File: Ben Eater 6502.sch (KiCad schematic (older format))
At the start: 13 parts, among them J1 PS/2 Keyboard, SW1 Reset, SW2 NMI, U1 W65C02SxP, U2 4011, U3 28C256, U4 AS6C62256A, U5 W65C22SxP

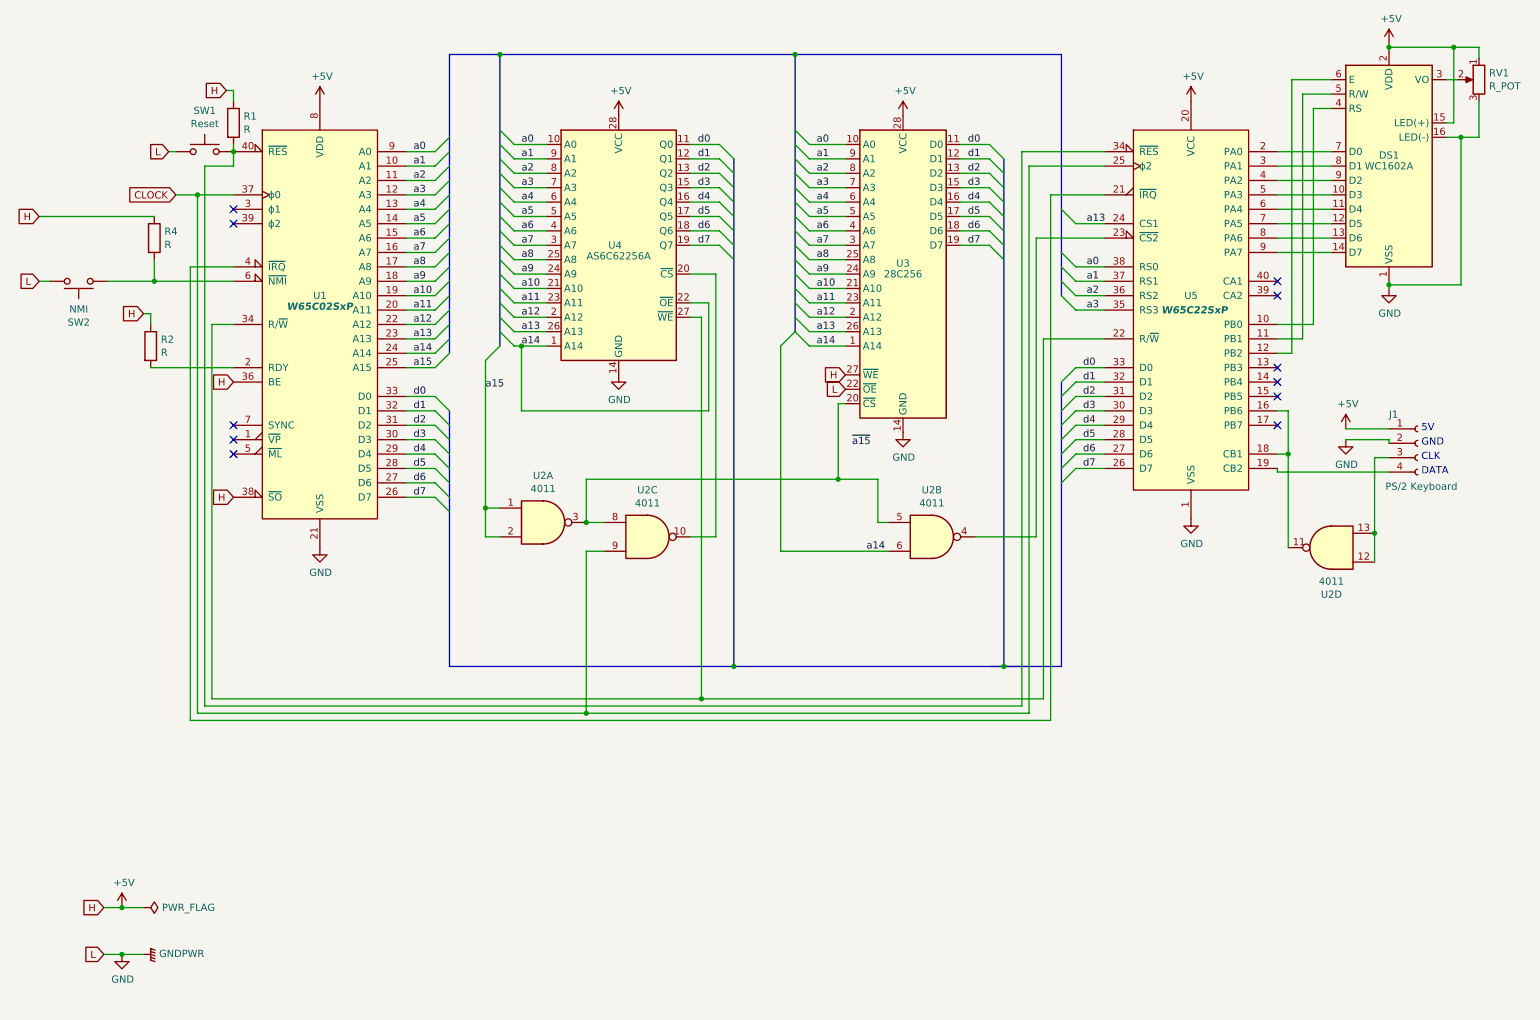
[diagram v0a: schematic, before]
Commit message: Add 74HC74 flip-flop to PS/2 keyboard data
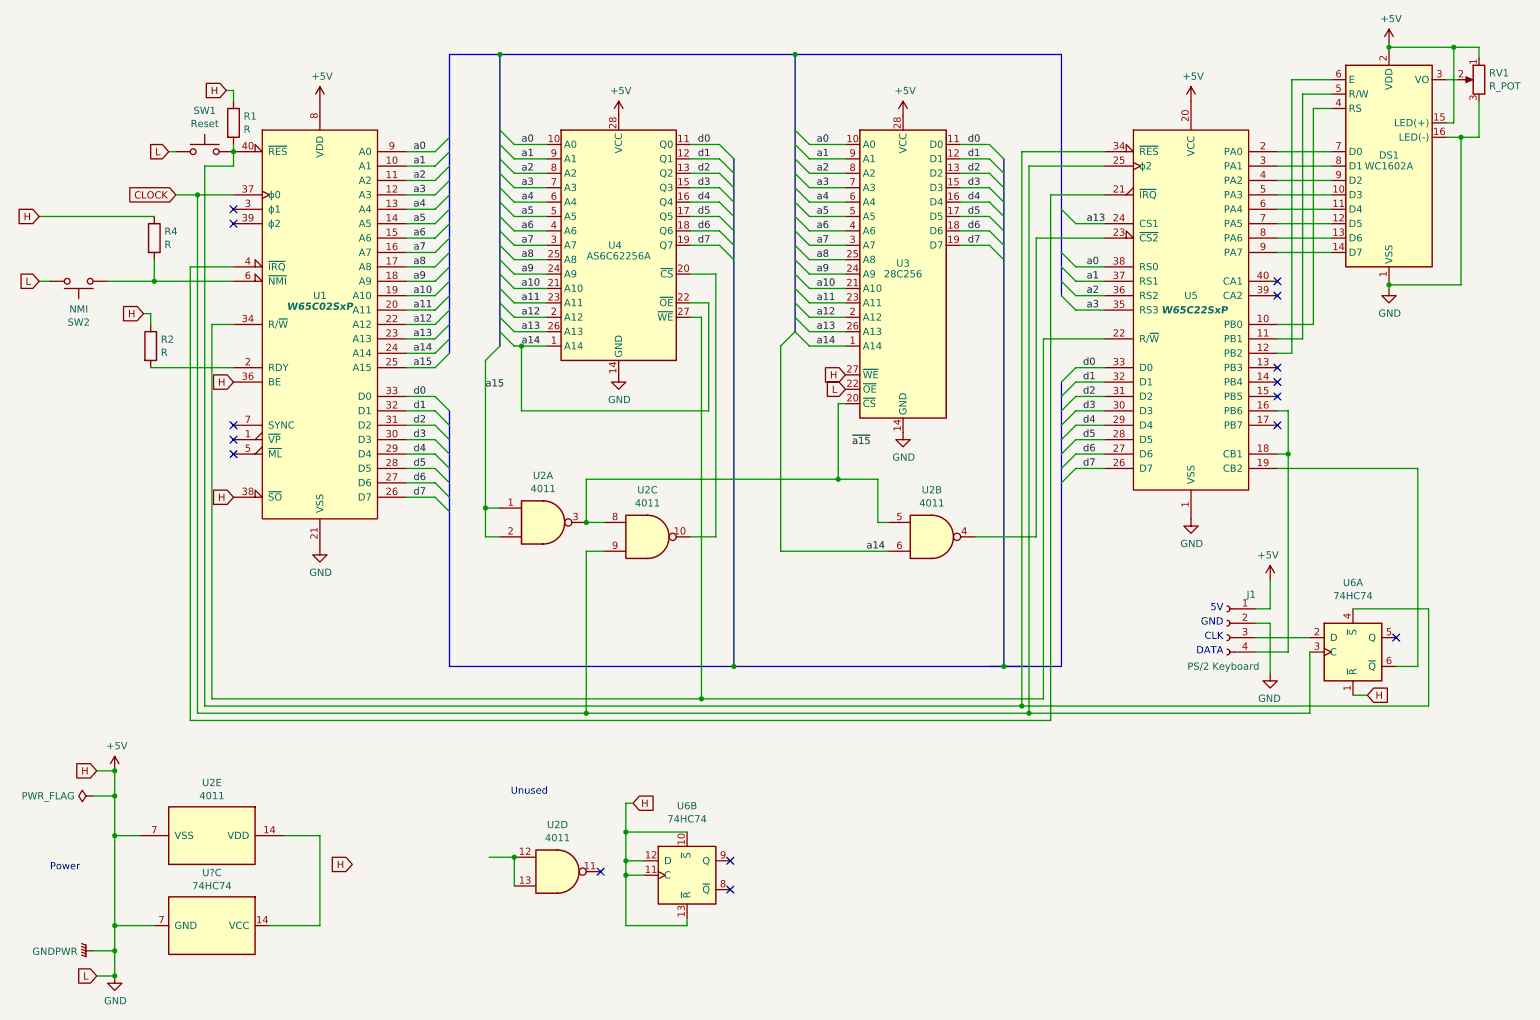
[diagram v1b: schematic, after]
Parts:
- added unit 5 of U2
- added U6, U?: 74HC74, symbol 74xx:74HC74
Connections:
- net GND is gone; now on net +5V: DS1.1 (VSS), DS1.16 (LED(-)), J1.2 (Pin_2), RV1.3, SW1.1, SW2.2, U1.21 (VSS), U3.14 (GND), U3.22 (~OE), U4.14 (GND), U5.1 (VSS)
- net +5V: now also U2.7 (VSS), U6.1 (~R), U6.10 (~S), U6.11 (C), U6.12 (D), U6.13 (~R), U?.7 (GND)
- net CLOCK: now also U6.3 (C)
- net at R1.2, SW1.2, U1.40 (~RES)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: now also U6.4 (~S)
- net at U5.16 (PB6), U5.18 (CB1): now also J1.4 (Pin_4); no longer U2.11
- net at U5.19 (CB2): now also U6.6 (~Q); no longer J1.4 (Pin_4)
- net at U2.12, U2.13: no longer J1.3 (Pin_3)
- new net: J1.3 (Pin_3), U6.2 (D)
- new net: U2.14 (VDD), U?.14 (VCC)
- no-connect marks 11 -> 15
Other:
- note added: "Power"
- note added: "Unused"
- moved on the sheet: J1, U2D

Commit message: Stage 6b
Use a 74HC74 on the ps/2 clock line to avoid the 6522 SR mode 011 bug.

See http://forum.6502.org/viewtopic.php?p=2310#p2310
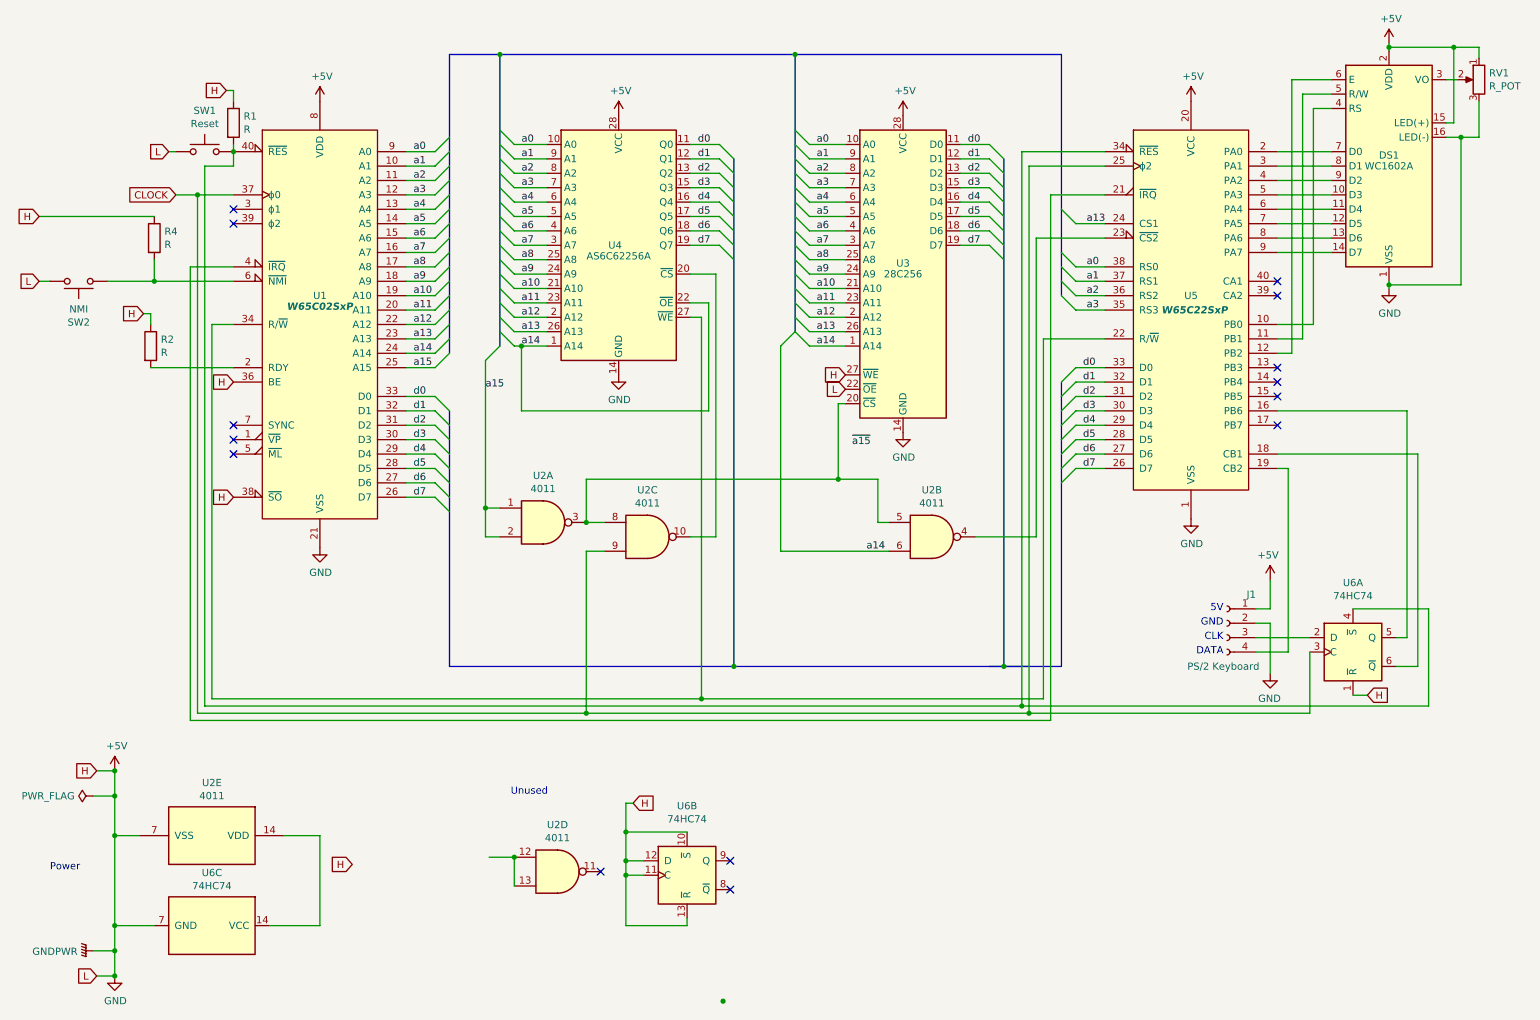
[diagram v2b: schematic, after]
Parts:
- gave numbers to parts that had none: 1
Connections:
- net at U6.6 (~Q): now also U5.18 (CB1); no longer U5.19 (CB2)
- net at U6.5 (Q): now also U5.16 (PB6)
- new net: J1.4 (Pin_4), U5.19 (CB2)
- no-connect marks 15 -> 14
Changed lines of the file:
@@
 DATA
 Wire Wire Line
-	9425 3800 9350 3800
-Wire Wire Line
-	9350 3500 9425 3500
-Wire Wire Line
-	9425 3500 9425 3800
-Connection ~ 9425 3800
+	9425 3900 9350 3900
 NoConn ~ 9350 3600
 NoConn ~ 9350 3400
@@
 	9200 5175 9425 5175
 Wire Wire Line
-	9425 3800 9425 5175
+	9425 3900 9425 5175
 Wire Wire Line
 	7625 5600 9575 5600
@@
 	9575 5600 9575 5175
 Connection ~ 7625 5600
-Wire Wire Line
-	9350 3900 10325 3900
-Wire Wire Line
-	10325 3900 10325 5275
 Wire Wire Line
 	10325 5275 10175 5275
@@
 Wire Wire Line
 	9875 5475 9975 5475
-NoConn ~ 10175 5075
 $Comp
 L 4xxx:4011 U2
@@
 $EndComp
 $Comp
-L 74xx:74HC74 U?
+L 74xx:74HC74 U6
 U 3 1 60B009B5
 P 1950 7075
-F 0 "U?" V 1583 7075 50  0000 C CNN
+F 0 "U6" V 1583 7075 50  0000 C CNN
 F 1 "74HC74" V 1674 7075 50  0000 C CNN
 F 2 "" H 1950 7075 50  0001 C CNN
@@
 Wire Wire Line
 	1275 6175 1275 6000
-Wire Bus Line
-	7850 1025 7850 2700
-Wire Bus Line
-	5575 1750 5575 5275
-Wire Bus Line
-	7850 3300 7850 5275
-Wire Bus Line
-	7450 1750 7450 5275
-Wire Bus Line
-	3600 3500 3600 5275
-Wire Bus Line
-	6000 1025 6000 2950
-Wire Bus Line
-	3950 1025 3950 3050
-Wire Bus Line
-	3600 1025 3600 3100
 Text Notes 825  6700 0    50   ~ 0
 Power
 Text Notes 4025 6175 0    50   ~ 0
 Unused
+Wire Wire Line
+	10325 3800 10325 5275
+Wire Wire Line
+	9350 3800 10325 3800
+Wire Wire Line
+	10250 3500 10250 5075
+Wire Wire Line
+	10250 5075 10175 5075
+Wire Wire Line
+	9350 3500 10250 3500
+Wire Bus Line
+	7850 1025 7850 2700
+Wire Bus Line
+	5575 1750 5575 5275
+Wire Bus Line
+	7850 3300 7850 5275
+Wire Bus Line
+	7450 1750 7450 5275
+Wire Bus Line
+	3600 3500 3600 5275
+Wire Bus Line
+	6000 1025 6000 2950
+Wire Bus Line
+	3950 1025 3950 3050
+Wire Bus Line
+	3600 1025 3600 3100
+Connection ~ 5500 7600
 $EndSCHEMATC

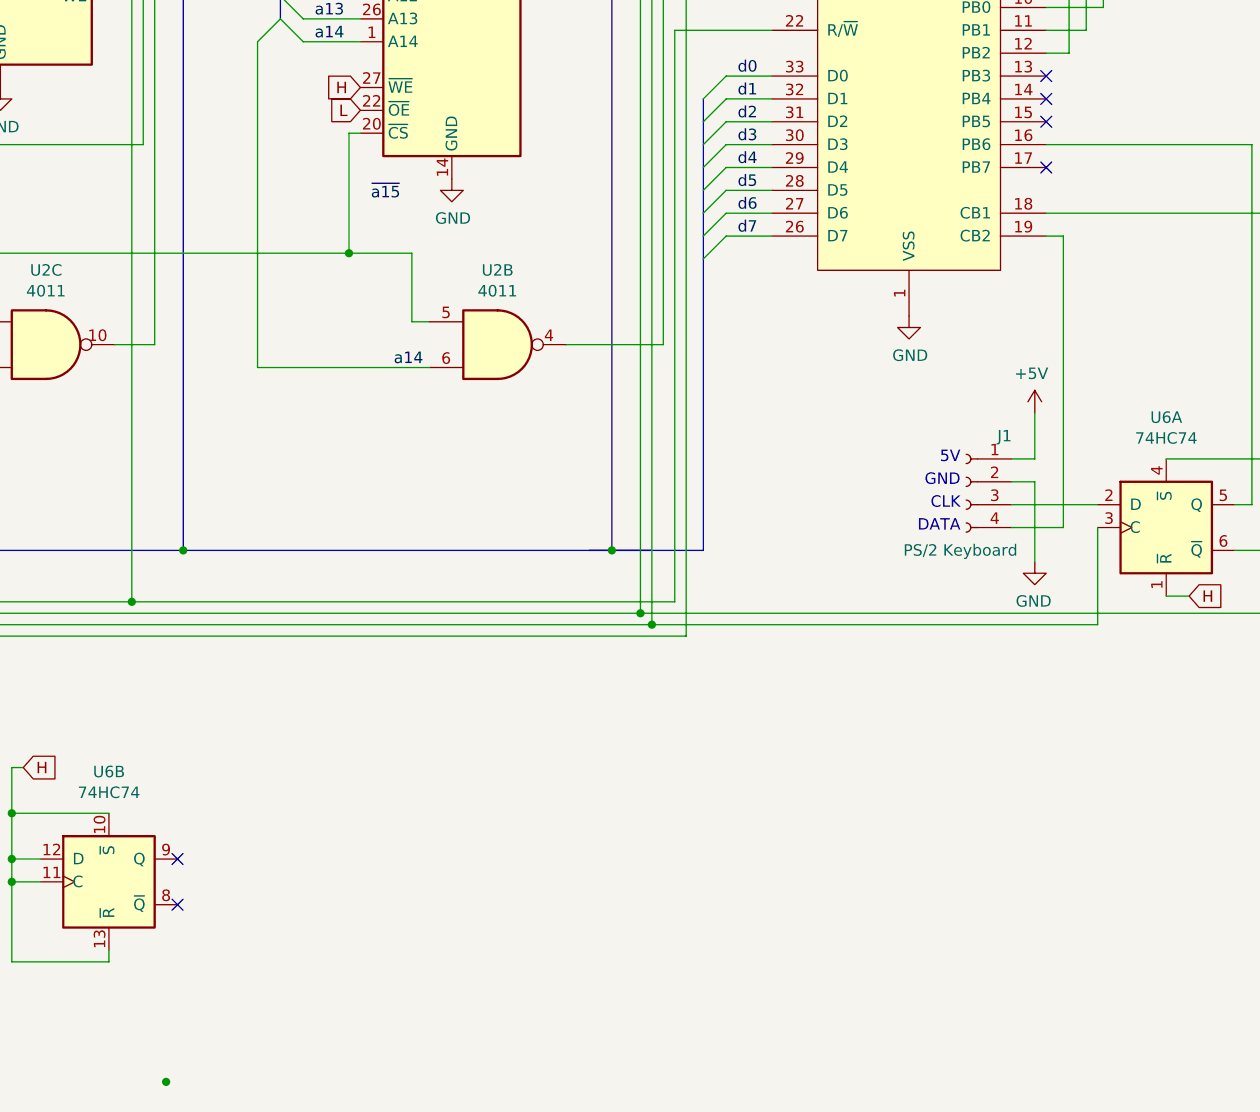
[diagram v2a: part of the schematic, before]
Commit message: Stage 6c
Connect PB7 to ps/2 clock line so we can pull it low to request host->
device comms
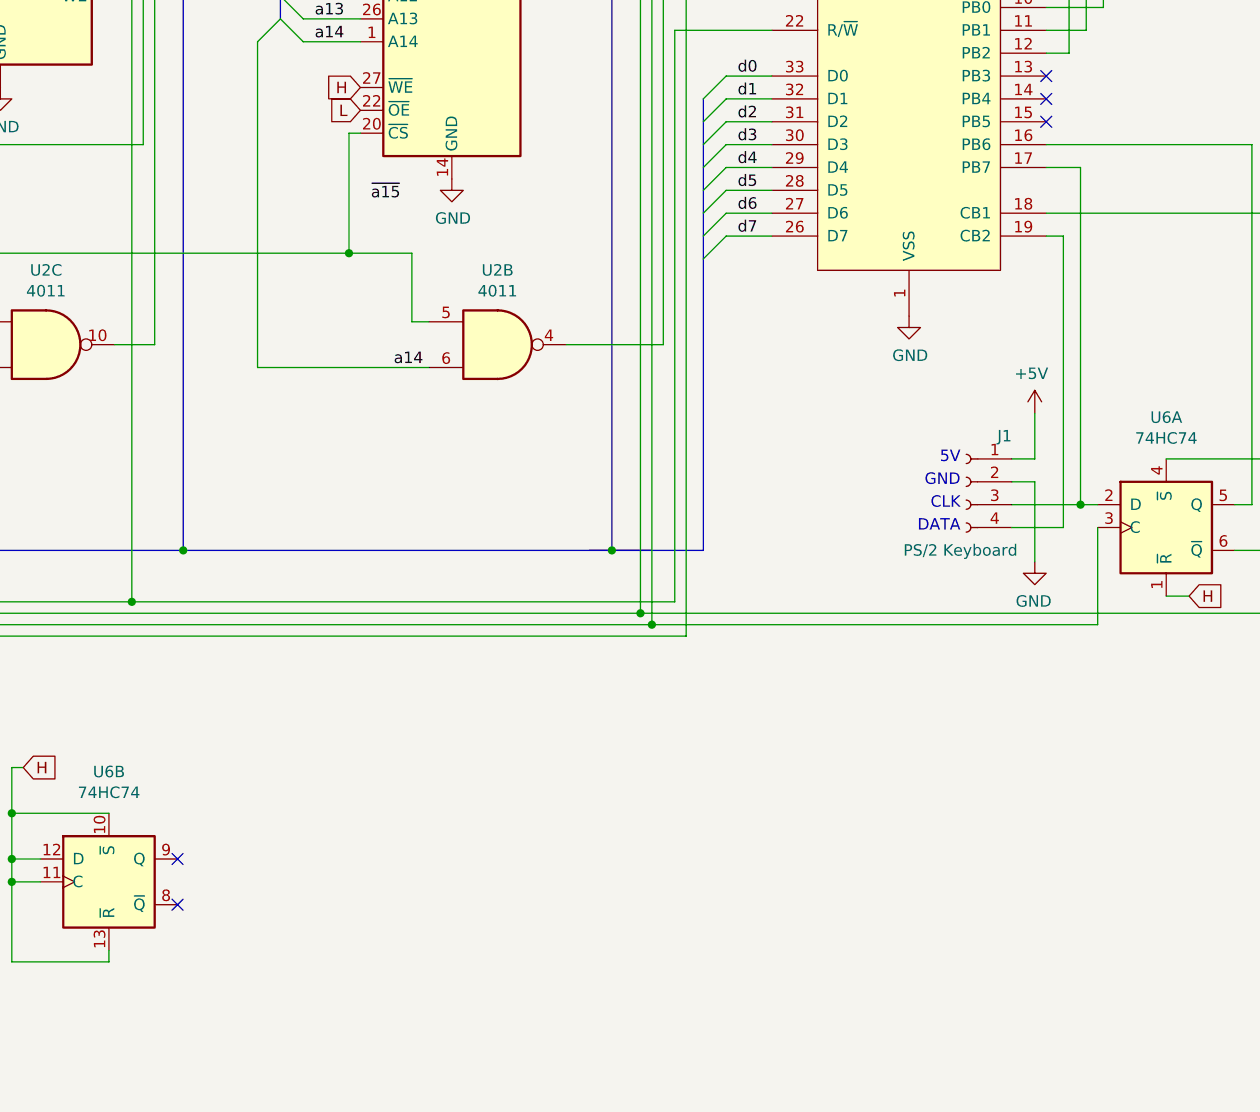
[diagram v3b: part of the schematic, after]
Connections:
- net at U5.17 (PB7): now also J1.3 (Pin_3), U6.2 (D)
- no-connect marks 14 -> 13
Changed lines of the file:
@@
 encoding utf-8
 Sheet 1 1
-Title "Ben Eater 6502 - Stage 6a"
+Title "Ben Eater 6502 - Stage 6c"
 Date "2021-03-22"
 Rev ""
@@
 Wire Wire Line
 	9425 3900 9350 3900
-NoConn ~ 9350 3600
 NoConn ~ 9350 3400
 NoConn ~ 9350 3300
@@
 	9300 4975 9300 5325
 Wire Wire Line
-	9200 5075 9575 5075
+	9200 5075 9500 5075
 Wire Wire Line
 	9200 5175 9425 5175
@@
 Wire Wire Line
 	9350 3500 10250 3500
+Wire Wire Line
+	9350 3600 9500 3600
+Wire Wire Line
+	9500 3600 9500 5075
 Wire Bus Line
 	7850 1025 7850 2700
@@
 Wire Bus Line
 	3600 1025 3600 3100
-Connection ~ 5500 7600
+Connection ~ 9500 5075
+Wire Wire Line
+	9500 5075 9575 5075
 $EndSCHEMATC
